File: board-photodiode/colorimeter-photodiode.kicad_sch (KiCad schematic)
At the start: 2 parts, among them J1 Conn_02x02_Counter_Clockwise

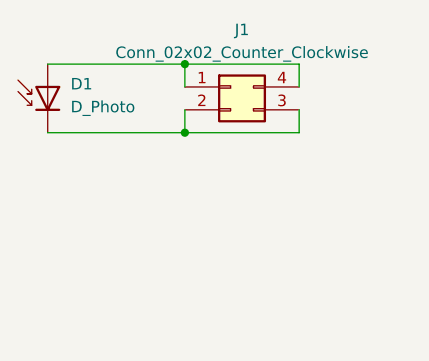
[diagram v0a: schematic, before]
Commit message: Change PD, LED boards to match pinout on main board
Added ground connections to both
Changed Photodiode to have 3x2 connector
Changed LED to common anode
Added new symbol & footprint for common anode RGB LED

Signed-off-by: Ioan Dragomir <ioan.dragomir@analog.com>
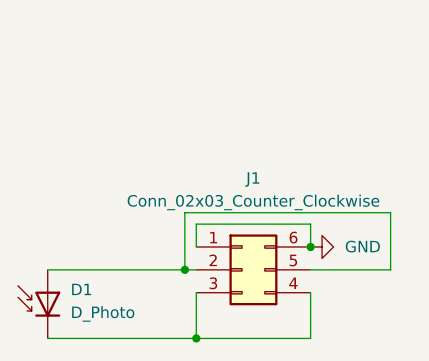
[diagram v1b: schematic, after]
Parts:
- removed J1: Conn_02x02_Counter_Clockwise, Connector_PinSocket_2.54mm:PinSocket_2x02_P2.54mm_Horizontal, symbol Connector_Generic:Conn_02x02_Counter_Clockwise
- added J1: Conn_02x03_Counter_Clockwise, Connector_PinSocket_2.54mm:PinSocket_2x03_P2.54mm_Horizontal, symbol Connector_Generic:Conn_02x03_Counter_Clockwise
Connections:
- net at D1.2 (A): now also J1.2 (Pin_2), J1.5 (Pin_5)
- net at D1.1 (K): now also J1.3 (Pin_3), J1.4 (Pin_4)
- new net GND: J1.1 (Pin_1), J1.6 (Pin_6)
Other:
- moved on the sheet: D1
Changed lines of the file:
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@@
 (kicad_sch (version 20230121) (generator eeschema)
   (paper "A4")
-  (junction (at 77.47 44.45) (diameter 0) (color 0 0 0 0)
+  (junction (at 78.74 74.93) (diameter 0) (color 0 0 0 0)
   )
-  (junction (at 77.47 52.07) (diameter 0) (color 0 0 0 0)
+  (junction (at 77.47 67.31) (diameter 0) (color 0 0 0 0)
   )
-  (wire (pts (xy 62.23 52.07) (xy 77.47 52.07))
+  (junction (at 91.44 64.77) (diameter 0) (color 0 0 0 0)
+  )
+  (wire (pts (xy 78.74 64.77) (xy 78.74 62.23))
     (stroke (width 0) (type default))
   )
-  (wire (pts (xy 62.23 44.45) (xy 77.47 44.45))
+  (wire (pts (xy 62.23 74.93) (xy 78.74 74.93))
     (stroke (width 0) (type default))
   )
-  (wire (pts (xy 90.17 44.45) (xy 77.47 44.45))
+  (wire (pts (xy 77.47 67.31) (xy 78.74 67.31))
     (stroke (width 0) (type default))
   )
-  (wire (pts (xy 77.47 52.07) (xy 77.47 49.53))
+  (wire (pts (xy 91.44 69.85) (xy 91.44 74.93))
     (stroke (width 0) (type default))
   )
-  (wire (pts (xy 90.17 49.53) (xy 90.17 52.07))
+  (wire (pts (xy 78.74 62.23) (xy 91.44 62.23))
     (stroke (width 0) (type default))
   )
-  (wire (pts (xy 77.47 44.45) (xy 77.47 46.99))
+  (wire (pts (xy 78.74 74.93) (xy 78.74 69.85))
     (stroke (width 0) (type default))
   )
-  (wire (pts (xy 90.17 46.99) (xy 90.17 44.45))
+  (wire (pts (xy 91.44 62.23) (xy 91.44 64.77))
     (stroke (width 0) (type default))
   )
-  (wire (pts (xy 90.17 52.07) (xy 77.47 52.07))
+  (wire (pts (xy 91.44 67.31) (xy 100.33 67.31))
     (stroke (width 0) (type default))
   )
-  (symbol (lib_id "Connector_Generic:Conn_02x02_Counter_Clockwise") (at 82.55 46.99 0) (unit 1)
+  (wire (pts (xy 91.44 74.93) (xy 78.74 74.93))
+    (stroke (width 0) (type default))
+  )
+  (wire (pts (xy 62.23 67.31) (xy 77.47 67.31))
+    (stroke (width 0) (type default))
+  )
+  (wire (pts (xy 77.47 60.96) (xy 77.47 67.31))
+    (stroke (width 0) (type default))
+  )
+  (wire (pts (xy 100.33 67.31) (xy 100.33 60.96))
+    (stroke (width 0) (type default))
+  )
+  (wire (pts (xy 100.33 60.96) (xy 77.47 60.96))
+    (stroke (width 0) (type default))
+  )
+  (symbol (lib_id "power:GND") (at 91.44 64.77 90) (unit 1)
     (in_bom yes) (on_board yes) (dnp no) (fields_autoplaced)
-    (property "Reference" "J1" (at 83.82 40.64 0)
-      (effects (font (size 1.27 1.27)))
-    )
-    (property "Value" "Conn_02x02_Counter_Clockwise" (at 83.82 43.18 0)
-      (effects (font (size 1.27 1.27)))
-    )
-    (property "Footprint" "Connector_PinSocket_2.54mm:PinSocket_2x02_P2.54mm_Horizontal" (at 82.55 46.99 0)
+    (property "Reference" "#PWR01" (at 97.79 64.77 0)
       (effects (font (size 1.27 1.27)) hide)
     )
-    (property "Datasheet" "~" (at 82.55 46.99 0)
+    (property "Value" "GND" (at 95.25 64.77 90)
+      (effects (font (size 1.27 1.27)) (justify right))
+    )
+    (property "Footprint" "" (at 91.44 64.77 0)
+      (effects (font (size 1.27 1.27)) hide)
+    )
+    (property "Datasheet" "" (at 91.44 64.77 0)
       (effects (font (size 1.27 1.27)) hide)
     )
     (pin "1")
-    (pin "2")
-    (pin "3")
-    (pin "4")
     (instances
       (project "colorimeter-photodiode"
         (path "/4c8677fa-e18a-4aff-82a4-83e0de866429"
-          (reference "J1") (unit 1)
+          (reference "#PWR01") (unit 1)
         )
       )
     )
   )
-  (symbol (lib_id "Device:D_Photo") (at 62.23 46.99 90) (unit 1)
+  (symbol (lib_id "Device:D_Photo") (at 62.23 69.85 90) (unit 1)
     (in_bom yes) (on_board yes) (dnp no) (fields_autoplaced)
-    (property "Reference" "D1" (at 64.77 46.6725 90)
+    (property "Reference" "D1" (at 64.77 69.5325 90)
       (effects (font (size 1.27 1.27)) (justify right))
     )
-    (property "Value" "D_Photo" (at 64.77 49.2125 90)
+    (property "Value" "D_Photo" (at 64.77 72.0725 90)
       (effects (font (size 1.27 1.27)) (justify right))
     )
-    (property "Footprint" "LED_THT:LED_D3.0mm_Clear" (at 62.23 48.26 0)
+    (property "Footprint" "LED_THT:LED_D3.0mm_Clear" (at 62.23 71.12 0)
       (effects (font (size 1.27 1.27)) hide)
     )
-    (property "Datasheet" "~" (at 62.23 48.26 0)
+    (property "Datasheet" "~" (at 62.23 71.12 0)
       (effects (font (size 1.27 1.27)) hide)
     )
@@
         )
       )
+    )
+  )
+  (symbol (lib_id "Connector_Generic:Conn_02x03_Counter_Clockwise") (at 83.82 67.31 0) (unit 1)
+    (in_bom yes) (on_board yes) (dnp no)
+    (property "Reference" "J1" (at 85.09 57.15 0)
+      (effects (font (size 1.27 1.27)))
+    )
+    (property "Value" "Conn_02x03_Counter_Clockwise" (at 85.09 59.69 0)
+      (effects (font (size 1.27 1.27)))
+    )
+    (property "Footprint" "Connector_PinSocket_2.54mm:PinSocket_2x03_P2.54mm_Horizontal" (at 83.82 67.31 0)
+      (effects (font (size 1.27 1.27)) hide)
+    )
+    (property "Datasheet" "~" (at 83.82 67.31 0)
+      (effects (font (size 1.27 1.27)) hide)
+    )
+    (pin "1")
+    (pin "2")
+    (pin "3")
+    (pin "4")
+    (pin "5")
+    (pin "6")
+    (instances
+      (project "colorimeter-photodiode"
+        (path "/4c8677fa-e18a-4aff-82a4-83e0de866429"
+          (reference "J1") (unit 1)
+        )
+      )

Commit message: Reorder photodiode riser board pins
Signed-off-by: Ioan Dragomir <ioan.dragomir@analog.com>
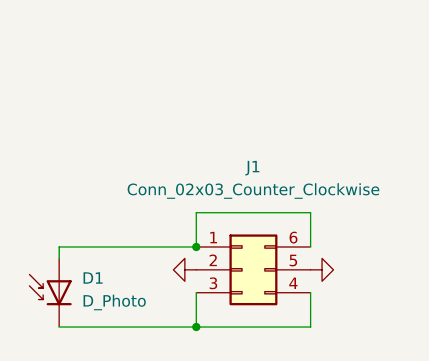
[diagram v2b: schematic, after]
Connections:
- net GND: now also J1.2 (Pin_2), J1.5 (Pin_5); no longer J1.1 (Pin_1), J1.6 (Pin_6)
- new net: D1.2 (A), J1.1 (Pin_1), J1.6 (Pin_6)
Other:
- moved on the sheet: D1
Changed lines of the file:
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@@
 (kicad_sch (version 20230121) (generator eeschema)
   (paper "A4")
-  (junction (at 78.74 74.93) (diameter 0) (color 0 0 0 0)
+  (junction (at 78.74 73.66) (diameter 0) (color 0 0 0 0)
   )
-  (junction (at 77.47 67.31) (diameter 0) (color 0 0 0 0)
+  (junction (at 78.74 64.77) (diameter 0) (color 0 0 0 0)
   )
-  (junction (at 91.44 64.77) (diameter 0) (color 0 0 0 0)
-  )
-  (wire (pts (xy 78.74 64.77) (xy 78.74 62.23))
+  (wire (pts (xy 63.5 64.77) (xy 63.5 66.04))
     (stroke (width 0) (type default))
   )
-  (wire (pts (xy 62.23 74.93) (xy 78.74 74.93))
+  (wire (pts (xy 63.5 73.66) (xy 78.74 73.66))
     (stroke (width 0) (type default))
   )
-  (wire (pts (xy 77.47 67.31) (xy 78.74 67.31))
+  (wire (pts (xy 91.44 69.85) (xy 91.44 73.66))
     (stroke (width 0) (type default))
   )
-  (wire (pts (xy 91.44 69.85) (xy 91.44 74.93))
+  (wire (pts (xy 78.74 69.85) (xy 78.74 73.66))
     (stroke (width 0) (type default))
   )
-  (wire (pts (xy 78.74 62.23) (xy 91.44 62.23))
+  (wire (pts (xy 91.44 73.66) (xy 78.74 73.66))
     (stroke (width 0) (type default))
   )
-  (wire (pts (xy 78.74 74.93) (xy 78.74 69.85))
+  (wire (pts (xy 63.5 64.77) (xy 78.74 64.77))
     (stroke (width 0) (type default))
   )
-  (wire (pts (xy 91.44 62.23) (xy 91.44 64.77))
+  (wire (pts (xy 78.74 60.96) (xy 78.74 64.77))
     (stroke (width 0) (type default))
   )
-  (wire (pts (xy 91.44 67.31) (xy 100.33 67.31))
+  (wire (pts (xy 91.44 64.77) (xy 91.44 60.96))
     (stroke (width 0) (type default))
   )
-  (wire (pts (xy 91.44 74.93) (xy 78.74 74.93))
+  (wire (pts (xy 91.44 60.96) (xy 78.74 60.96))
     (stroke (width 0) (type default))
   )
-  (wire (pts (xy 62.23 67.31) (xy 77.47 67.31))
-    (stroke (width 0) (type default))
-  )
-  (wire (pts (xy 77.47 60.96) (xy 77.47 67.31))
-    (stroke (width 0) (type default))
-  )
-  (wire (pts (xy 100.33 67.31) (xy 100.33 60.96))
-    (stroke (width 0) (type default))
-  )
-  (wire (pts (xy 100.33 60.96) (xy 77.47 60.96))
-    (stroke (width 0) (type default))
-  )
-  (symbol (lib_id "power:GND") (at 91.44 64.77 90) (unit 1)
+  (symbol (lib_id "power:GND") (at 91.44 67.31 90) (unit 1)
     (in_bom yes) (on_board yes) (dnp no) (fields_autoplaced)
-    (property "Reference" "#PWR01" (at 97.79 64.77 0)
+    (property "Reference" "#PWR02" (at 97.79 67.31 0)
       (effects (font (size 1.27 1.27)) hide)
     )
-    (property "Value" "GND" (at 95.25 64.77 90)
-      (effects (font (size 1.27 1.27)) (justify right))
+    (property "Value" "GND" (at 95.25 67.31 90)
+      (effects (font (size 1.27 1.27)) (justify right) hide)
     )
-    (property "Footprint" "" (at 91.44 64.77 0)
+    (property "Footprint" "" (at 91.44 67.31 0)
       (effects (font (size 1.27 1.27)) hide)
     )
-    (property "Datasheet" "" (at 91.44 64.77 0)
+    (property "Datasheet" "" (at 91.44 67.31 0)
       (effects (font (size 1.27 1.27)) hide)
     )
@@
       (project "colorimeter-photodiode"
         (path "/4c8677fa-e18a-4aff-82a4-83e0de866429"
-          (reference "#PWR01") (unit 1)
+          (reference "#PWR02") (unit 1)
         )
       )
     )
   )
-  (symbol (lib_id "Device:D_Photo") (at 62.23 69.85 90) (unit 1)
+  (symbol (lib_id "Device:D_Photo") (at 63.5 68.58 90) (unit 1)
     (in_bom yes) (on_board yes) (dnp no) (fields_autoplaced)
-    (property "Reference" "D1" (at 64.77 69.5325 90)
+    (property "Reference" "D1" (at 66.04 68.2625 90)
       (effects (font (size 1.27 1.27)) (justify right))
     )
-    (property "Value" "D_Photo" (at 64.77 72.0725 90)
+    (property "Value" "D_Photo" (at 66.04 70.8025 90)
       (effects (font (size 1.27 1.27)) (justify right))
     )
-    (property "Footprint" "LED_THT:LED_D3.0mm_Clear" (at 62.23 71.12 0)
+    (property "Footprint" "LED_THT:LED_D3.0mm_Clear" (at 63.5 69.85 0)
       (effects (font (size 1.27 1.27)) hide)
     )
-    (property "Datasheet" "~" (at 62.23 71.12 0)
+    (property "Datasheet" "~" (at 63.5 69.85 0)
       (effects (font (size 1.27 1.27)) hide)
     )
@@
     )
   )
+  (symbol (lib_id "power:GND") (at 78.74 67.31 270) (unit 1)
+    (in_bom yes) (on_board yes) (dnp no) (fields_autoplaced)
+    (property "Reference" "#PWR01" (at 72.39 67.31 0)
+      (effects (font (size 1.27 1.27)) hide)
+    )
+    (property "Value" "GND" (at 74.93 67.31 90)
+      (effects (font (size 1.27 1.27)) (justify right) hide)
+    )
+    (property "Footprint" "" (at 78.74 67.31 0)
+      (effects (font (size 1.27 1.27)) hide)
+    )
+    (property "Datasheet" "" (at 78.74 67.31 0)
+      (effects (font (size 1.27 1.27)) hide)
+    )
+    (pin "1")
+    (instances
+      (project "colorimeter-photodiode"
+        (path "/4c8677fa-e18a-4aff-82a4-83e0de866429"
+          (reference "#PWR01") (unit 1)
+        )
+      )
+    )
+  )
   (symbol (lib_id "Connector_Generic:Conn_02x03_Counter_Clockwise") (at 83.82 67.31 0) (unit 1)
     (in_bom yes) (on_board yes) (dnp no)
-    (property "Reference" "J1" (at 85.09 57.15 0)
+    (property "Reference" "J1" (at 85.09 55.88 0)
       (effects (font (size 1.27 1.27)))
     )
-    (property "Value" "Conn_02x03_Counter_Clockwise" (at 85.09 59.69 0)
+    (property "Value" "Conn_02x03_Counter_Clockwise" (at 85.09 58.42 0)
       (effects (font (size 1.27 1.27)))
     )
